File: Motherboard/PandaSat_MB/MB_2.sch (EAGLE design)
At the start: 142 parts, among them J1 503182-1852, J10 1445055-5, J2 10118194-0001LF, J3 DCJ0303, J4 1445055-5, J5 1445055-5, J6 1445055-5, J7 BK-18650, J8 1445055-5, J9 1445055-5, Q10 IRLML5103, Q11 IRLML5103, Q13 IRLML2803, Q14 IRLML2803, Q15 IRLML2803, Q16 IRLML5103, Q17 2N5088, Q2 32.768, U1 MAX706R, U11 DRV8848, U12 DRV8848, U2 LTC4121-4.2, U3 LSM9DS1, U4 PE014006, U5 MAX4372TEUK+T, U6 RFM23BP, U7 TPS54226PWPRPWP14_2P31X2P46-L, U8 ATSAMD51, U9 OKL-T3-W12, X1 BU-SMA-V

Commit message: aesthetic changes
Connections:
- new net N$22: R35.1, U5.RS-
- net VREG_IN: no longer R35.1, U5.RS-
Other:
- note added: "Batteries in 2s2p config"
- note removed: "Batterys in 2s2p config"
- moved on the sheet: C23, R35, U5

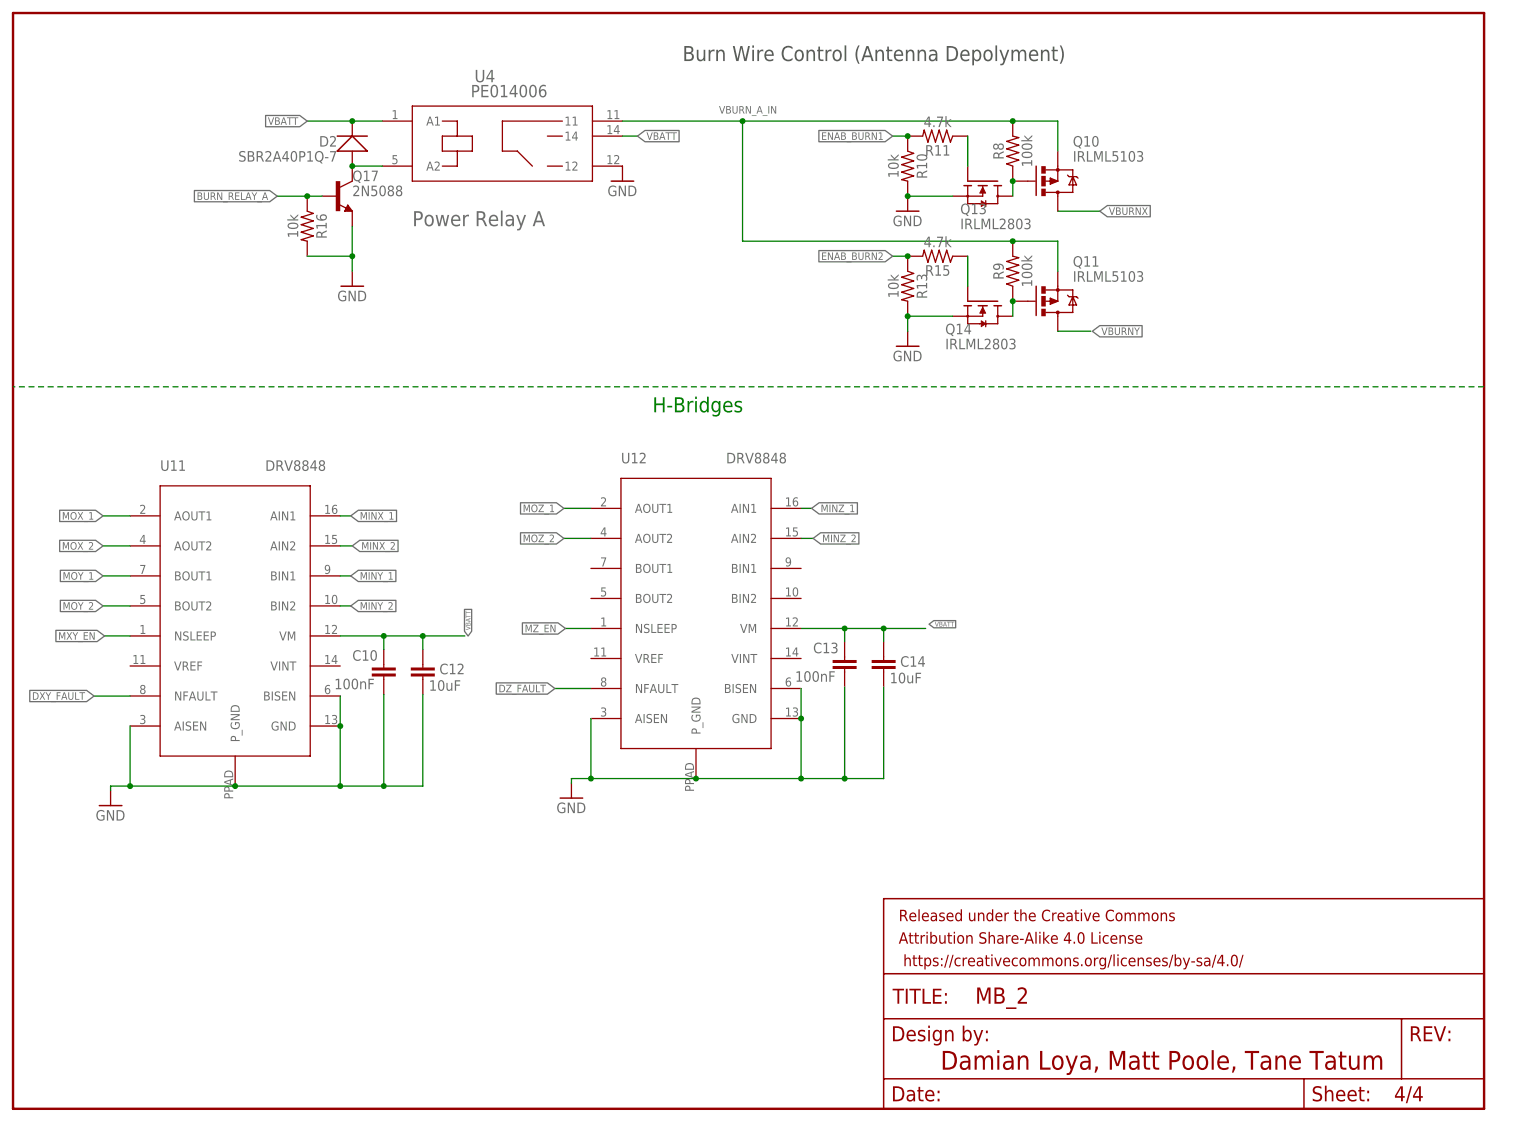
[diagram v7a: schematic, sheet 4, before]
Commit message: Added passives to H-Bridges
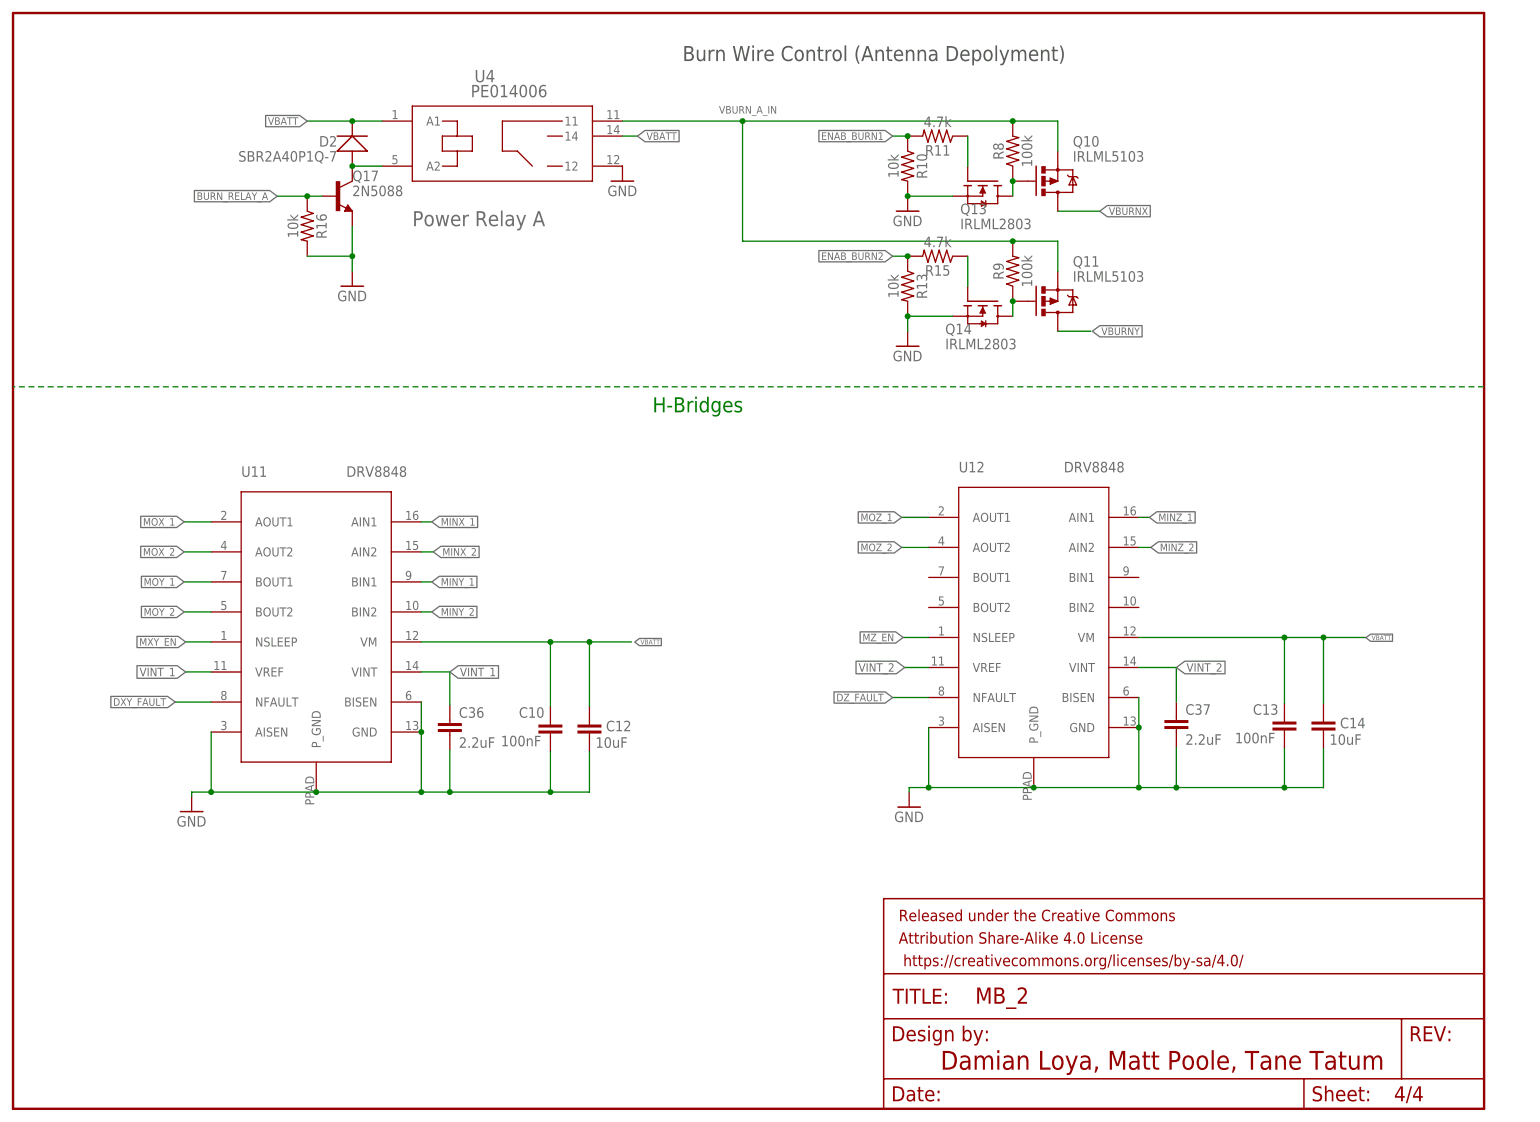
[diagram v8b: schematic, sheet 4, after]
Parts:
- added C36, C37: 2.2uF, SparkFun-Capacitors:CAP0603-CAP
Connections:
- new net VINT_1: C36.1, U11.VINT, U11.VREF
- new net VINT_2: C37.1, U12.VINT, U12.VREF
- net GND: now also C36.2, C37.2
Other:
- moved on the sheet: C10, C12, C13, C14, U11, U12
